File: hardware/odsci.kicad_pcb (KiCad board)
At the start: 4 copper layers, 50 x 70 mm, 35 parts, among them J1 USB_C_Receptacle, J2 Conn_01x03_Pin, J3 Conn_01x04_Pin, J4 Screw_Terminal_01x03, SW1 SW_Push, U1 TPS7A4701xRGW, U2 STM32F042K6Tx, U3 USBLC6-2SC6

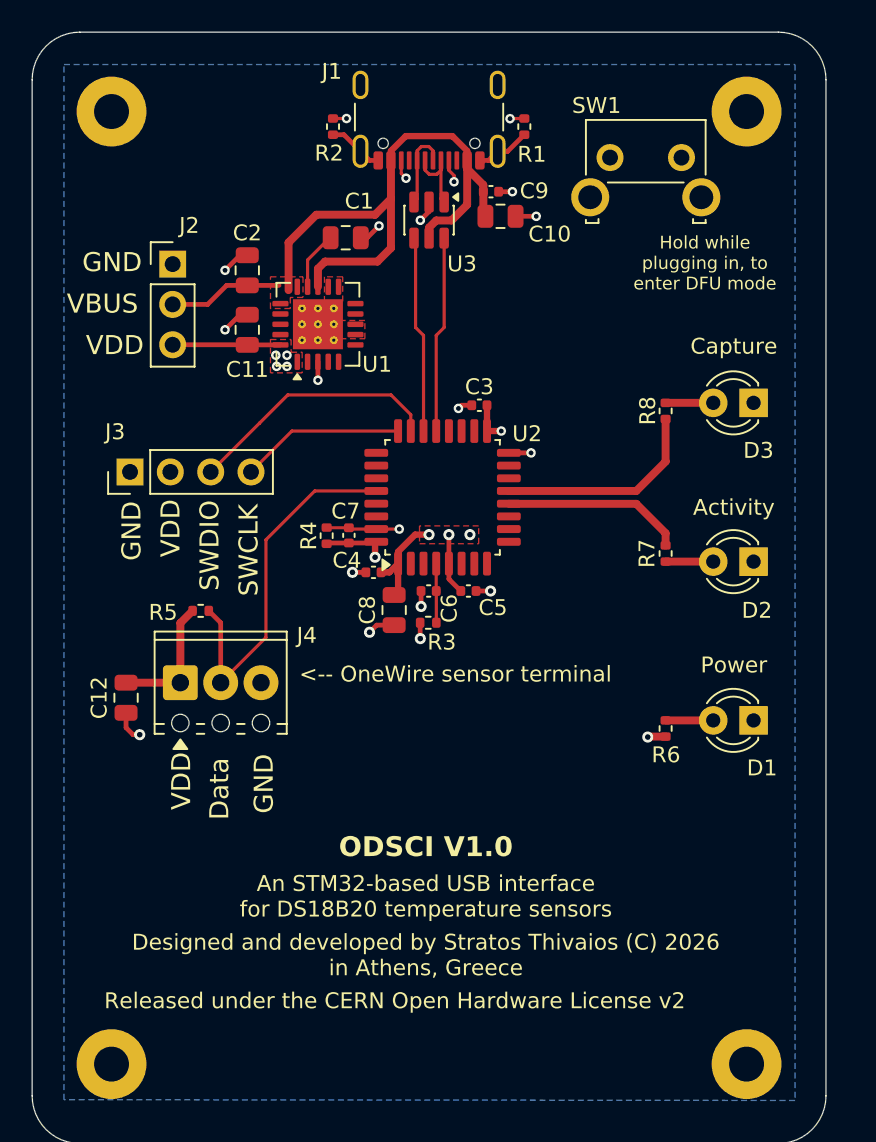
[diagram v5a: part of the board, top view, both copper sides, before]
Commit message: hardware: update silkscreen, tiny layout changes
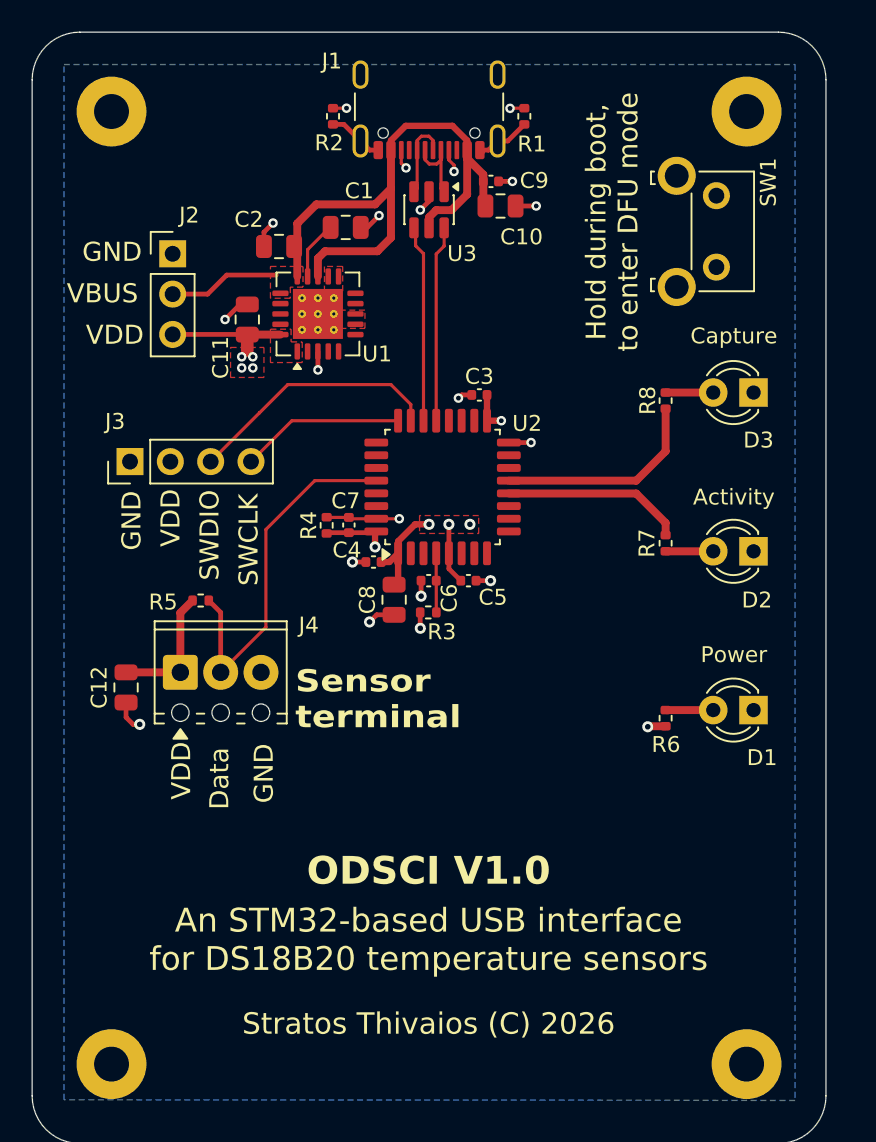
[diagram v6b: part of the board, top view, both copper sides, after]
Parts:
- moved SW1 7.12 mm to (168.6, 72.4), turned to -90 degrees
- moved C2 2.50 mm to (141.0, 75.6), turned to 0 degrees
- moved C10 0.65 mm to (155.0, 73.0)
- moved C12 0.65 mm to (131.4, 103.4)
- moved C4 0.65 mm to (147.0, 95.5)
- moved C7 0.65 mm to (145.4, 93.1)
- moved C8 0.65 mm to (148.3, 97.8)
- moved C9 0.65 mm to (154.4, 71.5)
- moved D1 0.65 mm to (170.9, 104.8)
- moved D2 0.65 mm to (170.9, 94.8)
- moved D3 0.65 mm to (170.9, 84.8)
- moved J1 0.65 mm to (150.5, 65.8)
- moved J4 0.65 mm to (134.8, 102.4)
- moved U1 0.65 mm to (143.5, 79.8)
- moved U2 0.65 mm to (151.3, 90.8)
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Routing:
- net Net-(U2-PB8): track 39.2 -> 34.5 mm
- net VDD: track 46.4 -> 47.4 mm
- net VBUS: track 46.8 -> 46.2 mm
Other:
- board text added: "Hold during boot, to enter DFU mode"
- board text added: "Sensor terminal"
- board text added: "Stratos Thivaios (C) 2026"
- board text added: "https://github.com/sthivaios/odsci"
- board text removed: "<-- OneWire sensor terminal"
- board text removed: "Designed and developed by Stratos Thivaios (C) 2026 in Athens, Greece"
- board text removed: "Hold while plugging in, to enter DFU mode"
